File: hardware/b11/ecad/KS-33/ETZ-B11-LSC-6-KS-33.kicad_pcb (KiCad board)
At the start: 2 copper layers, 131.5 x 85.8 mm, 0 parts

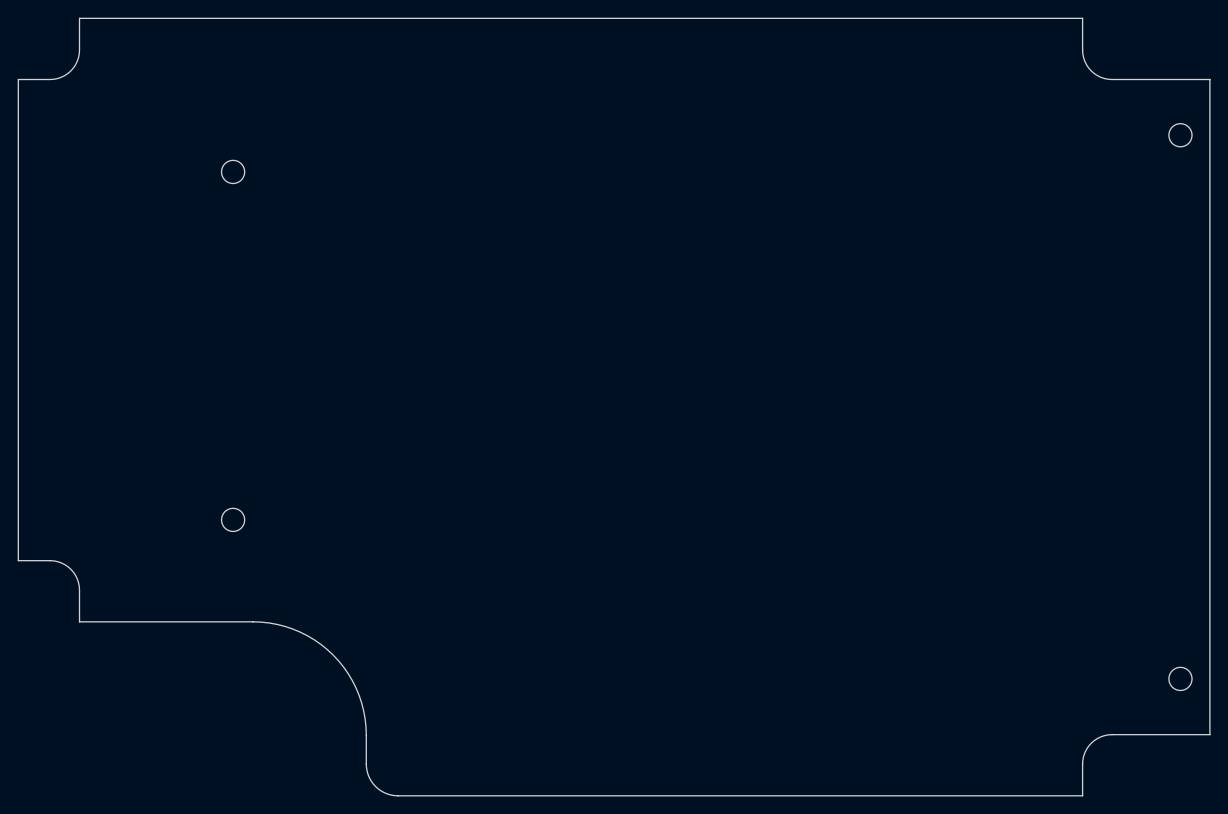
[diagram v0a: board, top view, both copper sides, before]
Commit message: fix(hardware/b11): fix 3D model paths, .kicad_pro files, KS-33 placement
- Update footprint model paths to \${KIPRJMOD}/../../../../lib/3d-models/
  so 3D models resolve correctly from ecad/{family}/ project directories
- Generate .kicad_pro for all 24 boards; remove dangling old ecad/ root .kicad_pro files
- Fix place-switch-sockets.py and place-switch-leds.py to read grid origin
  from board design settings instead of config constants
- Place KS-33 switch sockets and LEDs on all 4 carrier boards
- Propagate KiCad-normalised 1.6mm stackup across KS-33 SC boards

Co-Authored-By: Claude Sonnet 4.6 <noreply@anthropic.com>
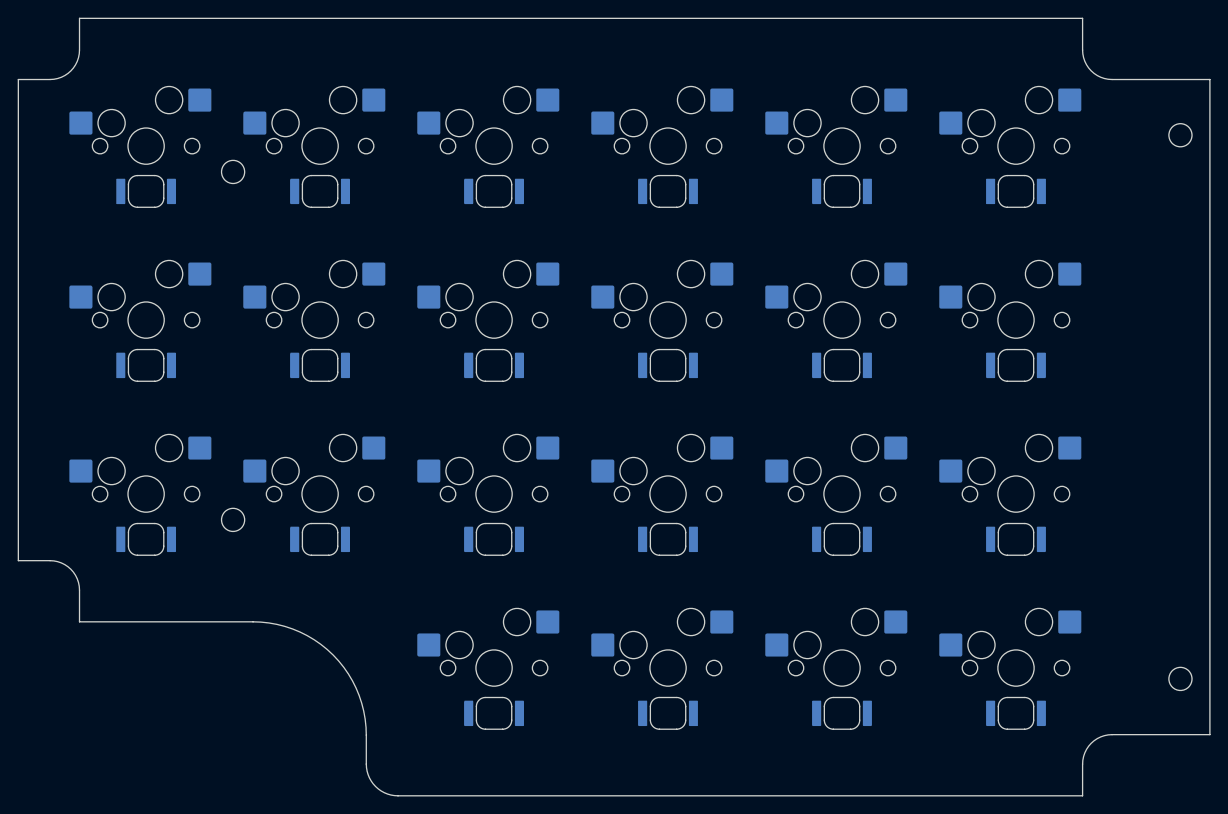
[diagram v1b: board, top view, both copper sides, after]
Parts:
- added LED1: 6028_LED, 6028_LED, F.Cu at (96.8, 78.3)
- added LED10: 6028_LED, 6028_LED, F.Cu at (154.4, 97.5)
- added LED11: 6028_LED, 6028_LED, F.Cu at (173.6, 97.5)
- added LED12: 6028_LED, 6028_LED, F.Cu at (192.8, 97.5)
- added LED13: 6028_LED, 6028_LED, F.Cu at (96.8, 116.7)
- added LED14: 6028_LED, 6028_LED, F.Cu at (116.0, 116.7)
- added LED15: 6028_LED, 6028_LED, F.Cu at (135.2, 116.7)
- added LED16: 6028_LED, 6028_LED, F.Cu at (154.4, 116.7)
- added LED17: 6028_LED, 6028_LED, F.Cu at (173.6, 116.7)
- added LED18: 6028_LED, 6028_LED, F.Cu at (192.8, 116.7)
- added LED19: 6028_LED, 6028_LED, F.Cu at (135.2, 135.9)
- added LED2: 6028_LED, 6028_LED, F.Cu at (116.0, 78.3)
- added LED20: 6028_LED, 6028_LED, F.Cu at (154.4, 135.9)
- added LED21: 6028_LED, 6028_LED, F.Cu at (173.6, 135.9)
- added LED22: 6028_LED, 6028_LED, F.Cu at (192.8, 135.9)
- added LED3: 6028_LED, 6028_LED, F.Cu at (135.2, 78.3)
- added LED4: 6028_LED, 6028_LED, F.Cu at (154.4, 78.3)
- added LED5: 6028_LED, 6028_LED, F.Cu at (173.6, 78.3)
- added LED6: 6028_LED, 6028_LED, F.Cu at (192.8, 78.3)
- added LED7: 6028_LED, 6028_LED, F.Cu at (96.8, 97.5)
- added LED8: 6028_LED, 6028_LED, F.Cu at (116.0, 97.5)
- added LED9: 6028_LED, 6028_LED, F.Cu at (135.2, 97.5)
- added SW1: KS-2P02B01-01-a, KS-2P02B01-01-a, F.Cu at (96.8, 73.3)
- added SW10: KS-2P02B01-01-a, KS-2P02B01-01-a, F.Cu at (154.4, 92.5)
- added SW11: KS-2P02B01-01-a, KS-2P02B01-01-a, F.Cu at (173.6, 92.5)
- added SW12: KS-2P02B01-01-a, KS-2P02B01-01-a, F.Cu at (192.8, 92.5)
- added SW13: KS-2P02B01-01-a, KS-2P02B01-01-a, F.Cu at (96.8, 111.7)
- added SW14: KS-2P02B01-01-a, KS-2P02B01-01-a, F.Cu at (116.0, 111.7)
- added SW15: KS-2P02B01-01-a, KS-2P02B01-01-a, F.Cu at (135.2, 111.7)
- added SW16: KS-2P02B01-01-a, KS-2P02B01-01-a, F.Cu at (154.4, 111.7)
- added SW17: KS-2P02B01-01-a, KS-2P02B01-01-a, F.Cu at (173.6, 111.7)
- added SW18: KS-2P02B01-01-a, KS-2P02B01-01-a, F.Cu at (192.8, 111.7)
- added SW19: KS-2P02B01-01-a, KS-2P02B01-01-a, F.Cu at (135.2, 130.9)
- added SW2: KS-2P02B01-01-a, KS-2P02B01-01-a, F.Cu at (116.0, 73.3)
- added SW20: KS-2P02B01-01-a, KS-2P02B01-01-a, F.Cu at (154.4, 130.9)
- added SW21: KS-2P02B01-01-a, KS-2P02B01-01-a, F.Cu at (173.6, 130.9)
- added SW22: KS-2P02B01-01-a, KS-2P02B01-01-a, F.Cu at (192.8, 130.9)
- added SW3: KS-2P02B01-01-a, KS-2P02B01-01-a, F.Cu at (135.2, 73.3)
- added SW4: KS-2P02B01-01-a, KS-2P02B01-01-a, F.Cu at (154.4, 73.3)
- added SW5: KS-2P02B01-01-a, KS-2P02B01-01-a, F.Cu at (173.6, 73.3)
- added SW6: KS-2P02B01-01-a, KS-2P02B01-01-a, F.Cu at (192.8, 73.3)
- added SW7: KS-2P02B01-01-a, KS-2P02B01-01-a, F.Cu at (96.8, 92.5)
- added SW8: KS-2P02B01-01-a, KS-2P02B01-01-a, F.Cu at (116.0, 92.5)
- added SW9: KS-2P02B01-01-a, KS-2P02B01-01-a, F.Cu at (135.2, 92.5)
